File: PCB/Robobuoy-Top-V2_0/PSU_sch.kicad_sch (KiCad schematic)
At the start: 49 parts, among them J201 Charge/On_Off, J202 Accu, Q202 A03401A, SW201 On/Off, U201 TLV61046ADB, U202 TP4056, U204 TLV61046ADB, U205 AP6685

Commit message: Start coding Bobobuoy
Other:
- note added: "C to small 1000uf fixed it"
- note added: "Fet not working here"
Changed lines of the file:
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@@
+		)
+	)
+	(text "Fet not working here"
+		(exclude_from_sim no)
+		(at 169.164 26.416 0)
+		(effects
+			(font
+				(size 1.27 1.27)
+			)
+		)
+	)
+	(text "C to small 1000uf fixed it"
+		(exclude_from_sim no)
+		(at 192.786 122.428 0)
+		(effects
+			(font
+				(size 1.27 1.27)
+			)
 		)
 	)

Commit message: More software on top
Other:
- note added: "3.3V psu not ok!"
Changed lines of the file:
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@@
+		)
+	)
+	(text "3.3V psu not ok!"
+		(exclude_from_sim no)
+		(at 140.208 101.346 0)
+		(effects
+			(font
+				(size 1.27 1.27)
+			)
 		)
 	)

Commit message: Top basic setup done
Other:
- note added: "Fet not working here Swap source and drain"
- note removed: "Fet not working here"
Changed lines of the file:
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@@
 		)
 	)
-	(text "Fet not working here"
+	(text "Fet not working here\nSwap source and drain\n"
 		(exclude_from_sim no)
 		(at 169.164 26.416 0)

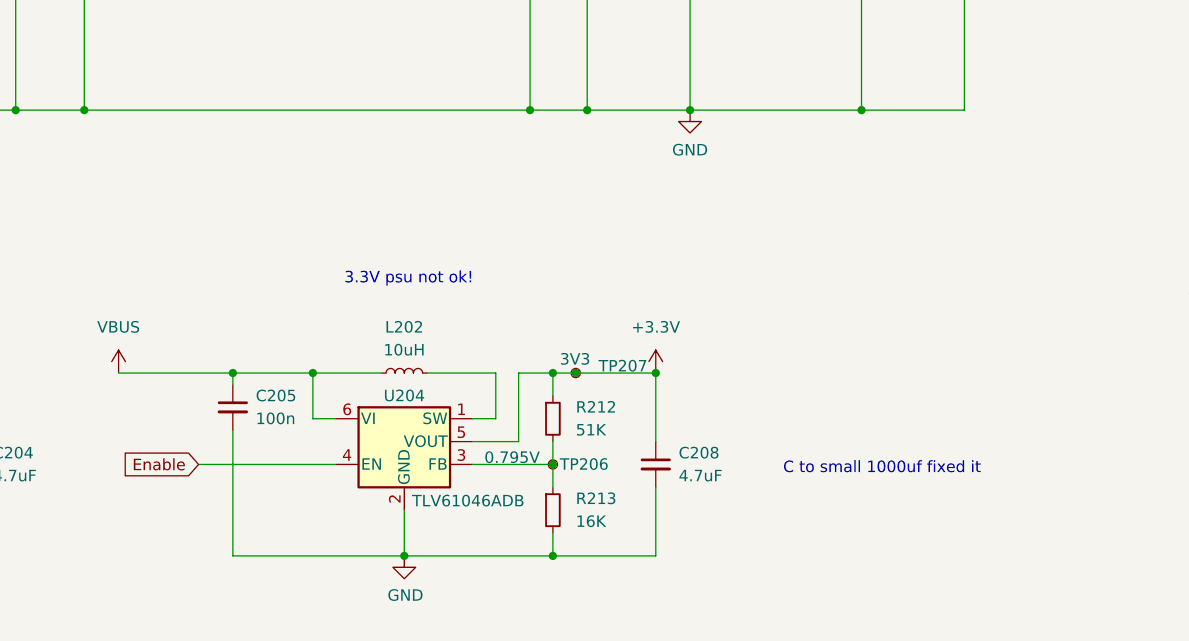
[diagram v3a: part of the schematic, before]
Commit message: Robobuoy top sources added Some KiCad notes added
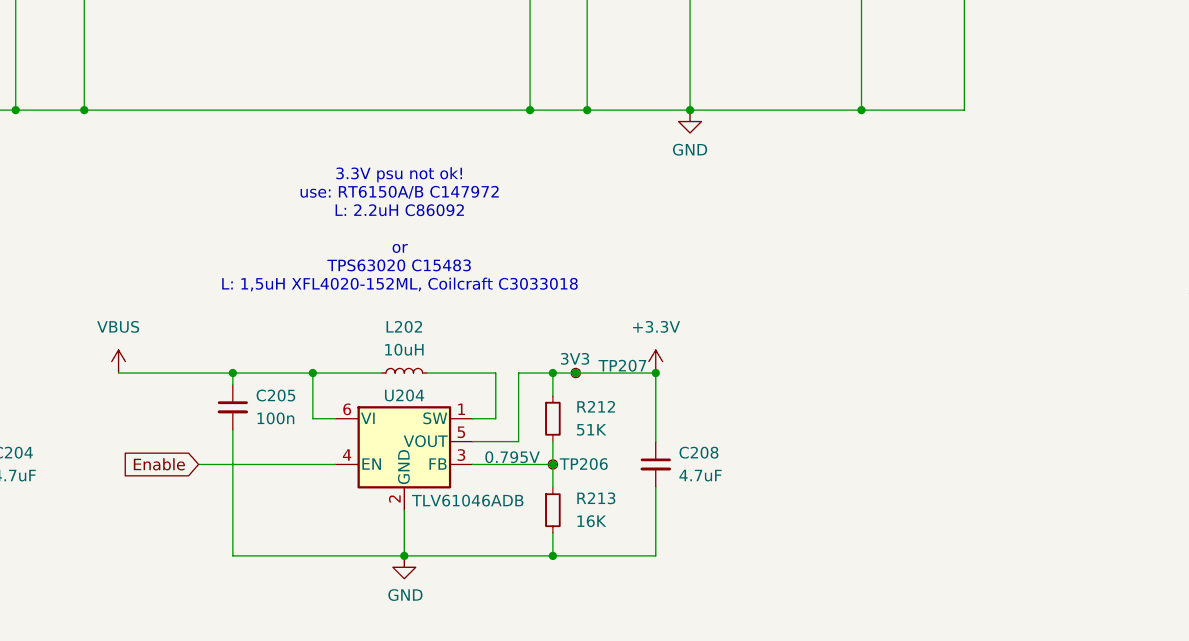
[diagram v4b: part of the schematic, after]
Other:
- note added: "3.3V psu not ok! use: RT6150A/B C147972 L: 2.2uH C86092 or TPS63020 C15483 L: 1,5uH XFL4020-152ML, Coilcraft C3033018"
- note removed: "3.3V psu not ok!"
- note removed: "C to small 1000uf fixed it"
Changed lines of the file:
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@@
 		)
 	)
-	(text "C to small 1000uf fixed it"
+	(text "3.3V psu not ok!\nuse: RT6150A/B C147972\nL: 2.2uH C86092\n\nor\nTPS63020 C15483\nL: 1,5uH XFL4020-152ML, Coilcraft C3033018"
 		(exclude_from_sim no)
-		(at 192.786 122.428 0)
+		(at 139.192 96.012 0)
 		(effects
 			(font
-				(size 1.27 1.27)
-			)
-		)
-	)
-	(text "3.3V psu not ok!"
-		(exclude_from_sim no)
-		(at 140.208 101.346 0)
-		(effects
-			(font

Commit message: Pc programm starting to code
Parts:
- removed D6: 5V, A_Device:LED_0805, symbol Device:LED_Small
- removed L201, L202: 10uH, A_Device:FTC252012S, symbol Device:L_Small
- removed R19: 1.5K, A_Device:R_0603, symbol Device:R_Small
- removed R212: 51K, A_Device:R_0603, symbol Device:R_Small
- removed R213: 16K, A_Device:R_0603, symbol Device:R_Small
- removed TP201, TP206: 0.795V, A_Pads_Pins:Testpad_1.4, symbol Connector:TestPoint_Small
- removed TP202: 5V, A_Pads_Pins:Testpoint_0.9x1.5, symbol Connector:TestPoint_Small
- removed TP207: 3V3, A_Pads_Pins:Testpad_1.4, symbol Connector:TestPoint_Small
- removed U201, U204: TLV61046ADB, Package_TO_SOT_SMD:SOT-23-6, symbol Regulator_Switching:TLV61046ADB
- added C211, C212, C213, C216, C217: 10u/10V, A_Passive:C_0805, symbol Device:C_Small
- added C214, C215: 100n, A_Device:C_0603, symbol Device:C_Small
- added L201: 1.5uH / 3.7A, A_Passive:L_2x2.5, symbol Device:L
- added R210: 1K, symbol Device:R_Small
- added U201: LM1117MP-3.3/TR, Package_TO_SOT_SMD:SOT-223, symbol Regulator_Linear:LM1117DT-3.3
- added U203: TPS63020DSJR, A_Confocal:QFN14_1, symbol NicE:TPS63021
- C204, C208: value 4.7uF -> 10u/10V; footprint A_Device:C_1206_(1.6) -> A_Passive:C_0805; LCSC C29823 -> C440198
- C205: value 100n -> 10u/10V; footprint A_Device:C_0603 -> A_Passive:C_0805; LCSC C14663 -> C440198
- R20, R201, R202: value 1K -> 4.7K
- R206: value 82K -> 10K; footprint A_Device:R_0603 -> (none); LCSC C23254 -> (none)
- R207: value 15K -> 1.2K; footprint A_Device:R_0603 -> (none); LCSC C22809 -> (none)
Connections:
- net +3.3V: now also C215.1, C216.1, C217.1, U201.2 (VO); no longer C208.1
- net +5V: now also C208.1, C211.1, C212.1, C213.1, C214.1, U201.3 (VI), U203.4 (Vout), U203.5 (Vout); no longer C204.1
- net Enable: now also U203.12 (EN)
- net GND: now also C211.2, C212.2, C213.2, C214.2, C215.2, C216.2, C217.2, U201.1 (GND), U203.15 (PGND), U203.2 (GND)
- net VBUS: now also C204.1, Q202.3 (S), U203.10 (Vin), U203.11 (Vin); no longer C201.1, Q202.1 (D)
- net at C207.1, J202.2 (Pin_2), R209.1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: now also Q202.1 (D); no longer Q202.3 (S)
- net at R207.1: now also R210.2, U203.3 (FB); no longer R206.2
- new net: L201.1, U203.8 (L1), U203.9 (L1)
- new net: L201.2, U203.6 (L2), U203.7 (L2)
- new net: R206.2, R210.1
- new net: C201.1, U203.1 (Vina), U203.13 (PS/SYNC)
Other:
- moved on the sheet: Q202
